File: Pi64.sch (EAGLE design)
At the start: 116 parts, among them J1 USB-MINIB-5PIN, J2 AVR_SPI, J3 FTDI_DEVICERA_SMT, J4 FTDI_DEVICERA_SMT, SW1 LEFT, SW2 RIGHT, SW3 PWR_SWITCH, SW8 OS102011MA1Q, U1 MIC7221, U2 MCP1642B-ADJ, U3 PAM2306AYPKE, U4 LM4875, U5 Mic5365-2.8Y, U7 AZV321, X2 HEADPHONE

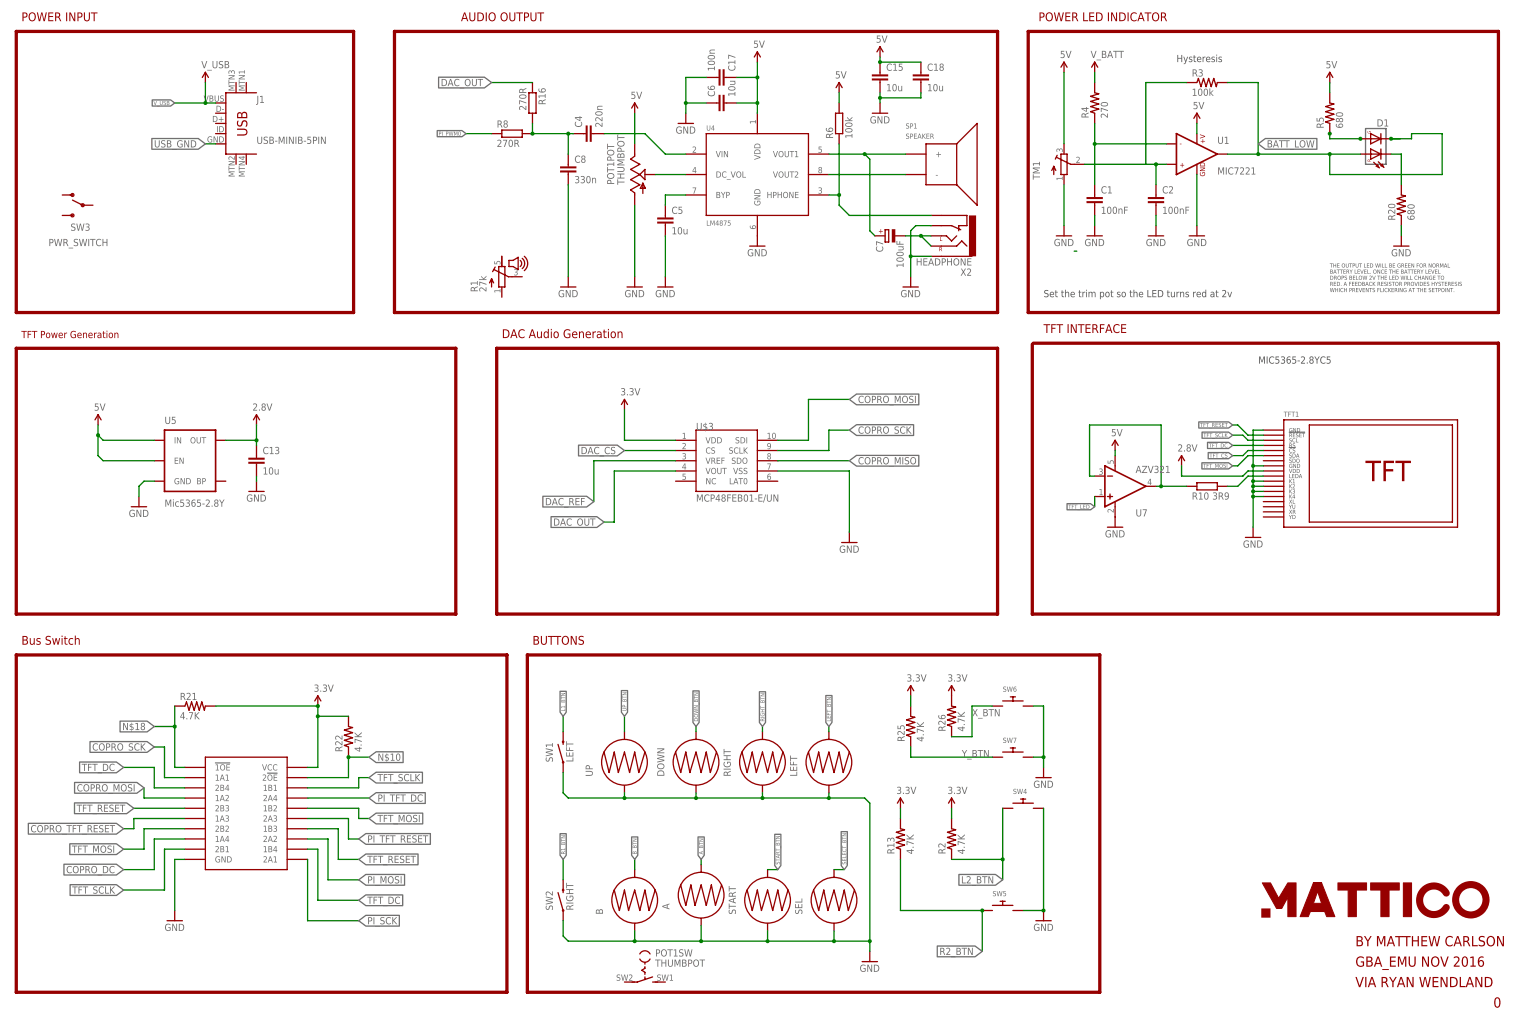
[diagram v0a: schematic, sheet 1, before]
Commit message: removed a lot of cruft and added STM32F
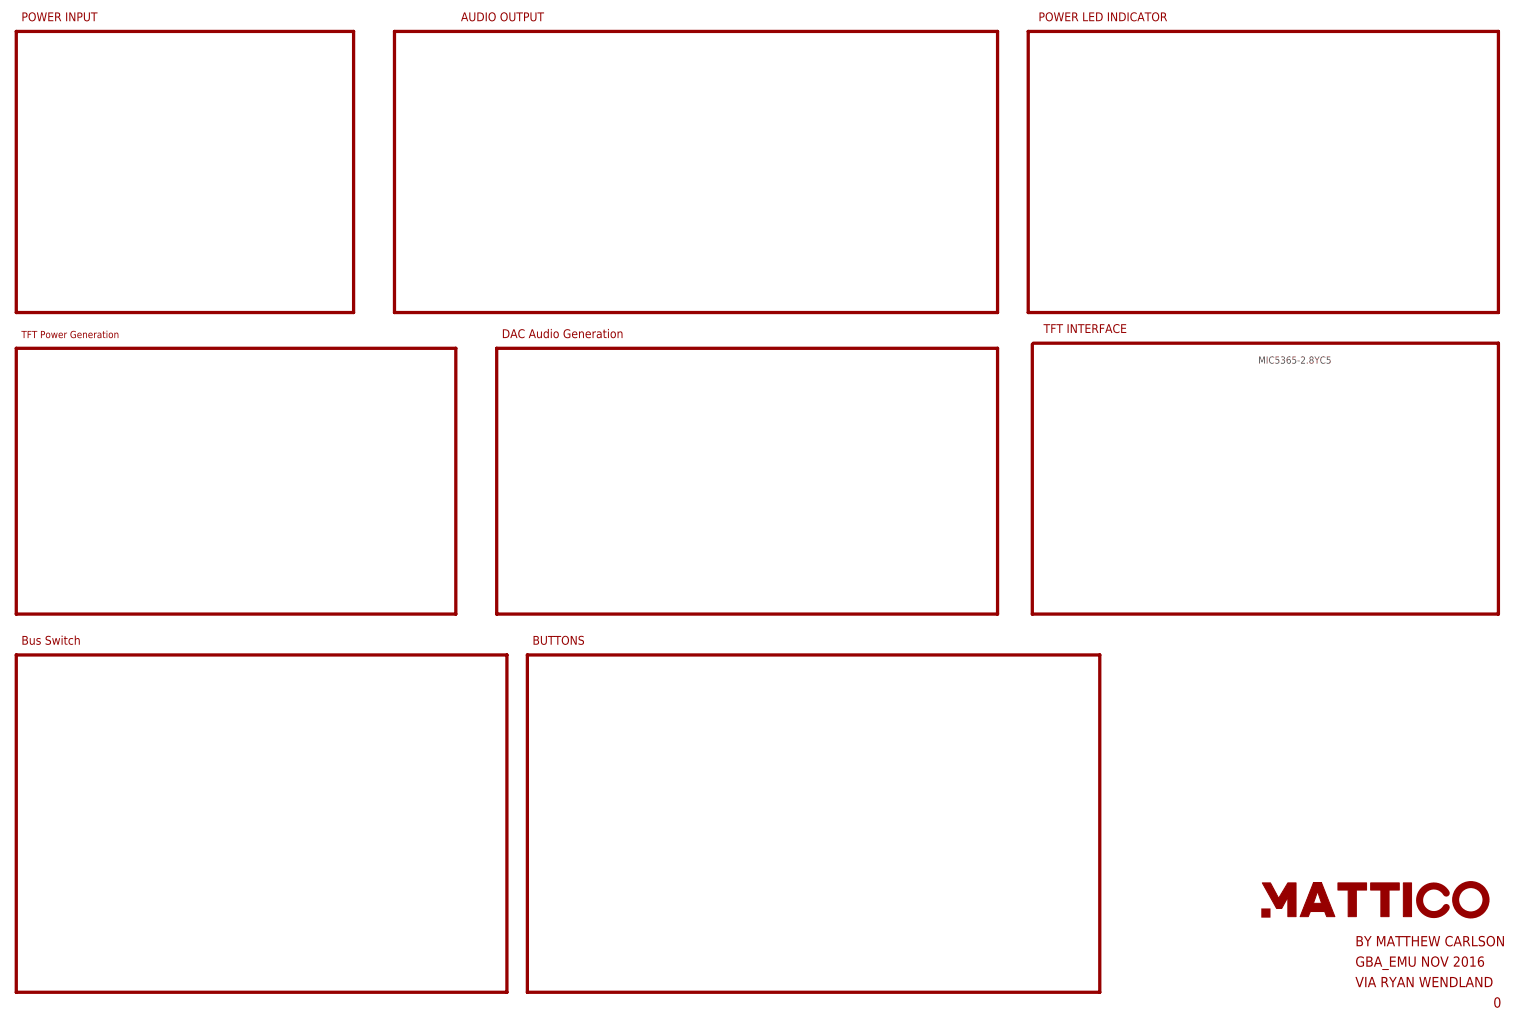
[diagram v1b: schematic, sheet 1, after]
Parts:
- removed A, B, DOWN, LEFT, RIGHT, UP: GBA_BTN_CONDUCTIVE, GBA:GBA_BTN_CONDUCTIVE
- removed BT1: (no value), custom:GBA_BATTERY
- removed C1, C2: 100nF, SparkFun-Capacitors:CAP0603-CAP
- removed C10: 1.0uF, SparkFun-Capacitors:1.0UF-16V-10%(0603)
- removed C11, C12: 22pF, SparkFun-Capacitors:22PF-50V-5%(0603)
- removed C13, C15, C18, C5, C6: 10u, rcl:C-EUC0805
- removed C14, C16: 47uF, SparkFun-Capacitors:47UF-10V-10%(TANT)
- removed C17: 100n, rcl:C-EUC0805
- removed C19: 100nF, SparkFun-Capacitors:10NF/10000PF-50V-10%(0603)
- removed C20, C21, C22, C23: 10uF, SparkFun-Capacitors:10UF-6.3V-20%(0603)
- removed C3: 100nF, SparkFun-Capacitors:10PF-50V-5%(0603)
- removed C4: 220n, rcl:C-EUC0805
- removed C7: 100uF, rcl:CPOL-EU153CLV-0405
- removed C8: 330n, rcl:C-EUC0805
- removed COPRO: MEGA16u2, adafruit:ATMEGA32U2-TQFP
- removed D1: DUAL_LED, custom:DUAL_LED
- removed D2, D3, D4, D7, D8: (no value), adafruit:DIODESOD-523
- removed D5, D6: DIODE_DFLS130L, custom:DIODE_DFLS130L
- removed FAN: (no value), SparkFun-Connectors:M02PTH
- removed J1: USB-MINIB-5PIN, SparkFun-Connectors:USB-MINIB-5PIN
- removed J2: AVR_SPI, SparkFun-Connectors:AVR_SPI_PRG_6PTH
- removed J3, J4: FTDI_DEVICERA_SMT, SparkFun-Connectors:FTDI_DEVICERA_SMT
- removed L1: 4.7uH, SparkFun-Passives:INDUCTORINDUCTOR_4.7UH
- removed L2, L3: 4.7µH/±30%/1.2A, SparkFun-Coils:INDUCTOR-CDRH-4.7UH
- removed POT1: THUMBPOT, adafruit:THUMBPOT
- removed R$1: 976kR, SparkFun-Resistors:820KOHM-1/10W-1%(0603)
- removed R$8: 430kR, SparkFun-Resistors:820KOHM-1/10W-1%(0603)
- removed R1: 27k, GBA:VOLUME
- removed R10: 3R9, rcl:R-EU_R0805
- removed R12: 1K, SparkFun-Resistors:1KOHM-1/10W-1%(0603)
- removed R13, R2, R21, R22, R25, R26: 4.7K, SparkFun-Resistors:4.7KOHM-1/10W-1%(0603)
- removed R16, R8: 270R, rcl:R-EU_R0805
- removed R17, R18: 22, SparkFun-Resistors:22OHM1/10W1%(0603)
- removed R19, R24, R27, R28: 10K, SparkFun-Resistors:10KOHM-1/10W-1%(0603)0603
- removed R20, R5: 680, SparkFun-Resistors:680OHM1/10W5%(0603)
- removed R23, R29, R3: 100k, SparkFun-Resistors:100KOHM-1/10W-1%(0603)
- removed R30, R31: (no value), SparkFun-Resistors:RESISTOR0805-RES
- removed R4: 270, SparkFun-Resistors:287OHM-1/10W-1%(0603)
- removed R6: 100k, rcl:R-EU_R0805
- removed SEL, START: BUTTON-CONDUCTIVESMD, SparkFun-Electromechanical:BUTTON-CONDUCTIVESMD
- removed SP1: SPEAKER, GBA:SPEAKER
- removed SW1: LEFT, GBA:BUTTON
- removed SW2: RIGHT, GBA:BUTTON
- removed SW3: PWR_SWITCH, GBA:PWR_SWITCH
- removed SW4, SW5: (no value), adafruit:SWITCH_PUSHBUTTONEVQ-PE
- removed SW6, SW7: (no value), adafruit:SWITCH_PUSHBUTTONSOFTTOUCHSMD_SJ
- removed SW8: OS102011MA1Q, adafruit:OS102011MA1Q
- removed T1: (no value), custom:TRANSISTOR_PNP_DRIVERMUN2111T1SC59-BEC
- removed TFT1: GBA_TFT, GBA:GBA_TFT
- removed TM1: (no value), adafruit:TRIMPOTTC33X
- removed U$1: CBT3244AD, custom:CBT3244AD
- removed U$3: MCP48FEB01-E/UN, custom:MCP48FEB01-E/UN
- removed U$5: CRYSTAL-ABLS, custom:CRYSTAL-ABLS
- removed U2: MCP1642B-ADJ, custom:MICROCHIP_MCP1642B-ADJ
- removed U3: PAM2306AYPKE, custom:PAM2306AYPKE
- removed U4: LM4875, texas:LM4875
- removed U5: Mic5365-2.8Y, SparkFun-PowerIC:V_REG_LDOSMD2
- removed U7: AZV321, GBA:AZV321
- removed X1: (no value), Adafruit_PowerBoost:MICROBUILDER_USB_TYPEAPTHFML
- removed X2: HEADPHONE, GBA:HEADPHONE
- U1: value MIC7221 -> STM32F103CBT6; device custom:SPARKFUN-ANALOGIC_MIC7221 -> custom:STM32F103CBT6
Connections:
- removed net BATT_LOW: D1.1, D1.3, D8.A, R3.2, U1.OUT1
- removed net COPRO_D+: R18.1
- removed net COPRO_D-: R17.1
- removed net COPRO_DC: COPRO.PB6(PCINT6), U$1.1A4
- removed net COPRO_MISO: COPRO.PB3(PDO/MISO/PCINT3), J2.1, U$3.SDO
- removed net COPRO_MOSI: COPRO.PB2(PDI/MOSI/PCINT2), J2.4, U$1.1A2, U$3.SDI
- removed net COPRO_RESET: COPRO./RESET(PC1), J2.5, R19.1
- removed net COPRO_RX: COPRO.PD2(INT2/AIN1/RXD1)
- removed net COPRO_SCK: COPRO.PB1(SCK/PCINT1), J2.3, U$1.1A1, U$3.SCLK
- removed net COPRO_TFT_RESET: COPRO.PB0(SS/PCINT0), U$1.1A3
- removed net COPRO_TX: COPRO.PD3(INT3/TXD1)
- removed net DAC_CS: COPRO.PB5(PCINT5), U$3.CS
- removed net DAC_OUT: R16.1, U$3.VOUT
- removed net DAC_REF: U$3.VREF
- removed net FAN_EN: R12.2
- removed net N$10: R22.1, U$1.2!OE
- removed net N$11: C5.1, U4.BYP
- removed net N$12: COPRO.PC2(AIN2/PCIN11), R28.1
- removed net N$13: C7.-, X2.LEFT, X2.RIGHT
- removed net N$14: C7.+, SP1.+, U4.VOUT1
- removed net N$15: SP1.-, U4.VOUT2
- removed net N$16: R6.1, U4.HPHONE, X2.2
- removed net N$18: R21.1, U$1.!1OE
- removed net N$19: COPRO.D-, R17.2
- removed net N$2: C4.1, C8.1, R16.2, R8.2
- removed net N$21: R10.2, TFT1.LEDA
- removed net N$22: COPRO.D+, R18.2
- removed net N$23: R$1.1, R$8.2, U2.VFB
- removed net N$24: R10.1, U7.-IN, U7.OUT
- removed net N$25: C10.1, COPRO.UCAP
- removed net N$28: C11.1, COPRO.XTAL1, U$5.P$2
- removed net N$29: C12.1, COPRO.XTAL2/PC0, U$5.P$1
- removed net N$3: D7.A, D8.C
- removed net N$31: D3.A, D4.C
- removed net N$32: L3.1, U3.LX2
- removed net N$33: D3.C, D7.C, R27.2, R28.2
- removed net N$34: L1.2, U2.SW
- removed net N$38: COPRO.PC7(ICP1/INT4/CLKO), R27.1
- removed net N$39: FAN.1, T1.C
- removed net N$4: C2.1, R3.1, TM1.S, U1.+IN1
- removed net N$40: R12.1, T1.B
- removed net N$44: COPRO.PD0(INT0/OC0B), R24.1
- removed net N$45: C14.+, D5.C, D6.C, L1.1, SW8G$1.P, U2.VIN
- removed net N$46: C19.1, R29.1, U3.EN2
- removed net N$47: L2.1, U3.LX1
- removed net N$49: R31.2, U3.FB1
- removed net N$5: C1.1, R4.1, U1.-IN1
- removed net N$50: R30.1, U3.FB2
- removed net N$6: D1.4, R5.1
- removed net N$7: D1.2, R20.2
- removed net N$8: POT1POT.S, U4.DC_VOL
- removed net N$9: C4.2, U4.VIN
- removed net PWR_DOWN: D2.A, D4.A, SW8G$1.S
- removed net PWR_UP: D2.C, R23.2, R24.2, U2.EN
- removed net TFT_CS: COPRO.PD4(INT5/AIN3), TFT1.!CS
- removed net TFT_DC: TFT1.RS, U$1.1B4, U$1.2B4
- removed net TFT_MOSI: TFT1.SDA, U$1.1B2, U$1.2B2
- removed net TFT_RESET: TFT1.!RESET, U$1.1B3, U$1.2B3
- removed net TFT_SCLK: TFT1.SCL, U$1.1B1, U$1.2B1
- removed net USB_GND: J1.GND
- removed net V_BATT: BT1.+, D6.A, R4.2
- removed net V_USB: D5.A, J1.VBUS
- new net +3V3: U1.VBAT, U1.VDDA, U1.VDD_1, U1.VDD_2, U1.VDD_3
- net 1.8V: no longer C20.1, L3.2, R30.2
- net 2.8V: no longer C13.1, TFT1.VDD, U5.OUT
- net 3.3V: no longer C21.1, COPRO.AVCC, COPRO.UVCC, COPRO.VCC, L2.2, R13.2, R2.2, R21.2, R22.2, R25.2, R26.2, R31.1, U$1.VCC, U$3.VDD
- net 5V: no longer C15.1, C16.+, C17.1, C18.1, C22.1, C23.1, C3.1, C6.2, FAN.2, J2.2, POT1POT.E, R$1.2, R19.2, R29.2, R5.2, R6.2, TM1.E, U1.+V, U2.VOUT, U3.EN1, U3.VIN1, U3.VIN2, U4.VDD, U5.EN, U5.IN, U7.V+, X1.VBUS
- net A_BTN: no longer A.2
- net B_BTN: no longer B.2
- net DOWN_BTN: no longer DOWN.2
- net GND: no longer A.1, B.1, BT1.-, C1.2, C10.2, C11.2, C12.2, C13.2, C14.-, C15.2, C16.-, C17.2, C18.2, C19.2, C2.2, C20.2, C21.2, C22.2, C23.2, C3.2, C5.2, C6.1, C8.2, COPRO.GND, COPRO.UGND, DOWN.1, J2.6, J3.GND, J4.GND, LEFT.1, POT1POT.A, R$8.1, R20.1, R23.1, RIGHT.1, SEL.1, START.1, SW1.1, SW2.1, SW4.P$2, SW5.P$2, SW6.P$2, SW7.P$2, T1.E, TFT1.GND@1, TFT1.GND@2, TFT1.K1, TFT1.K2, TFT1.K3, TFT1.K4, TM1.A, U$1.GND, U$3.VSS, U1.GND, U2.GND, U3.GND@1, U3.GND@2, U4.GND, U5.GND, U7.V-, UP.1, X1.GND, X2.1, X2.GND
- net L1_BTN: no longer SW1.2
- net L2_BTN: no longer R2.1, SW4.P$1
- net LEFT_BTN: no longer LEFT.2
- net PI_MOSI: no longer U$1.2A2
- net PI_PWM0: no longer R8.1
- net PI_SCK: no longer U$1.2A1
- net PI_TFT_DC: no longer U$1.2A4
- net PI_TFT_RESET: no longer U$1.2A3
- net R1_BTN: no longer SW2.2
- net R2_BTN: no longer R13.1, SW5.P$1
- net RIGHT_BTN: no longer RIGHT.2
- net SELECT_BTN: no longer SEL.2
- net START_BTN: no longer START.2
- net TFT_LED: no longer U7.+IN
- net UP_BTN: no longer UP.2
- net X_BTN: no longer R26.1, SW6.P$1
- net Y_BTN: no longer R25.1, SW7.P$1
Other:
- note removed: "C16 as close to VOUT as possible"
- note removed: "Hysteresis"
- note removed: "Power Or'ing"
- note removed: "Set the trim pot so the LED turns red at 2v"
- note removed: "THE OUTPUT LED WILL BE GREEN FOR NORMAL BATTERY LEVEL. ONCE THE BATTERY LEVEL DROPS BELOW 2V THE LED WILL CHANGE TO RED. A FEEDBACK RESISTOR PROVIDES HYSTERESIS WHICH PREVENTS FLICKERING AT THE SETPOINT."
- moved on the sheet: TP1, TP2, TP3, TP4, TP5, TP6, TP7

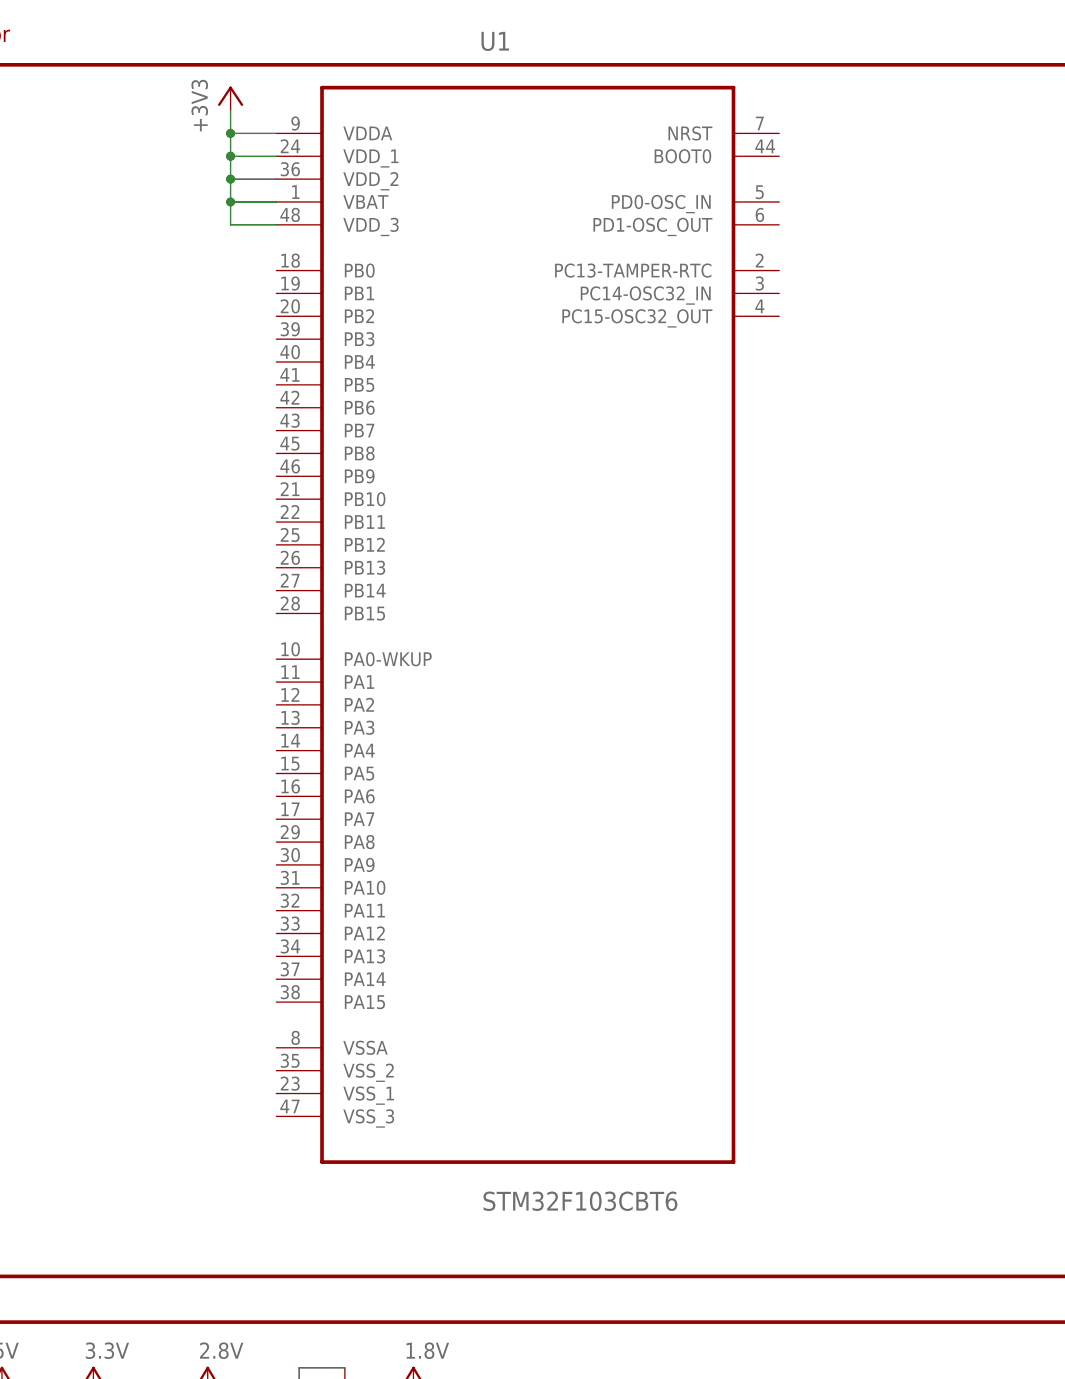
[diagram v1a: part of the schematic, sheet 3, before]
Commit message: Added PWR and GND to STM32
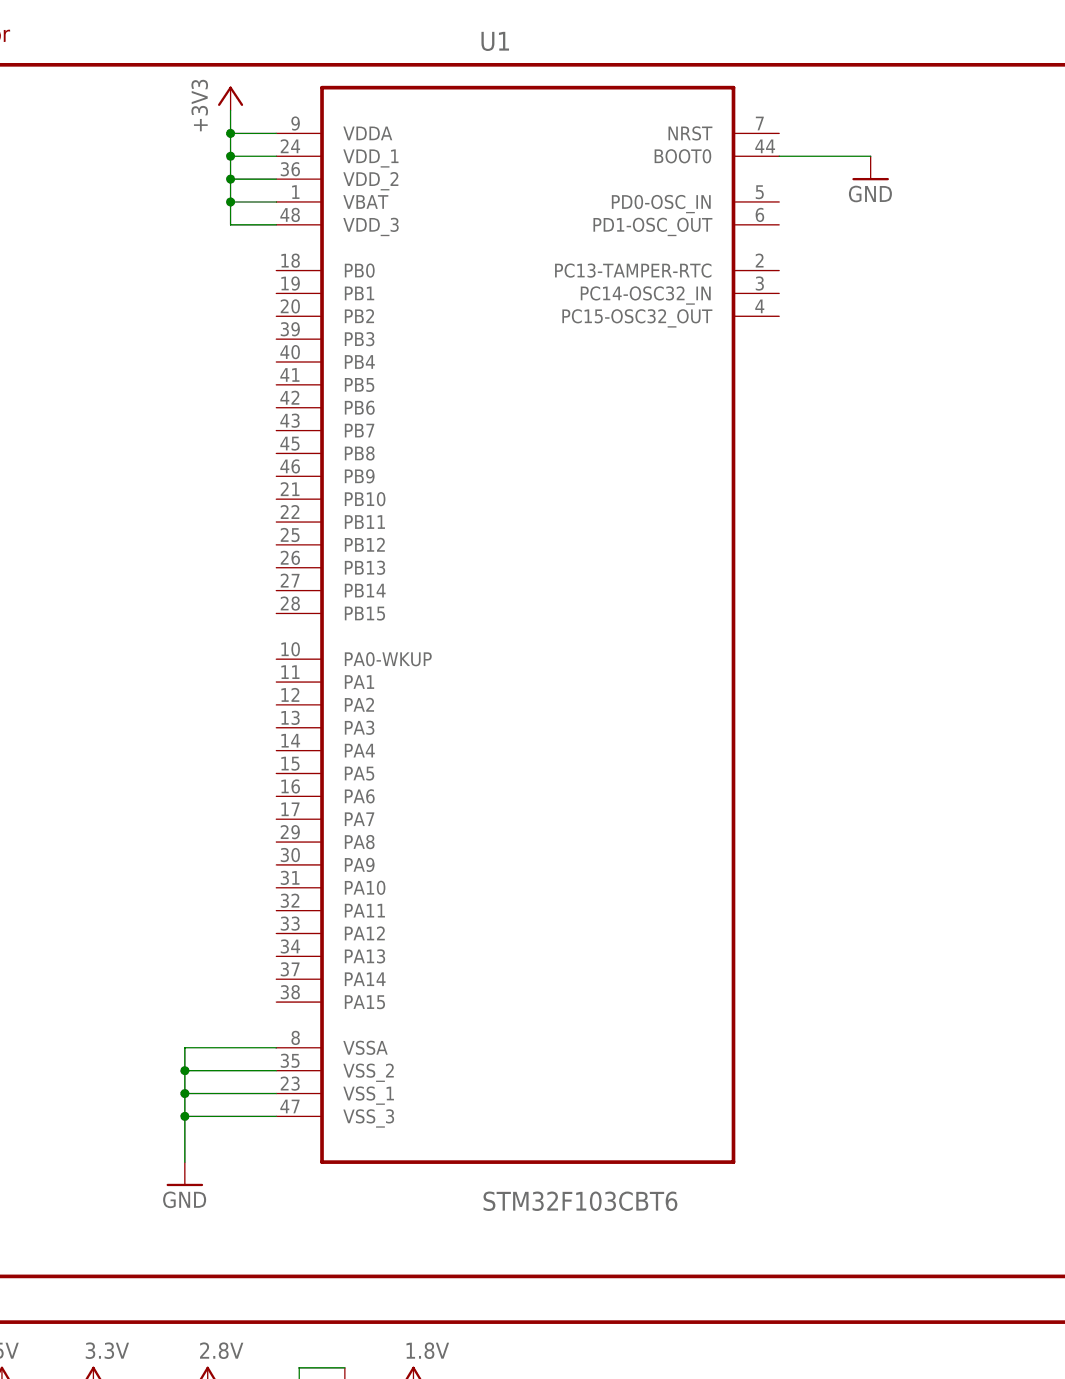
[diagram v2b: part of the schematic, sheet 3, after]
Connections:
- net GND: now also U1.BOOT0, U1.VSSA, U1.VSS_1, U1.VSS_2, U1.VSS_3
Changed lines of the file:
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@@
 <part name="U1" library="custom" deviceset="STM32F103CBT6" device=""/>
 <part name="3V3_STM" library="supply1" library_urn="urn:adsk.eagle:library:371" deviceset="+3V3" device=""/>
+<part name="GND1" library="SparkFun-Aesthetics" deviceset="GND" device=""/>
+<part name="GND2" library="SparkFun-Aesthetics" deviceset="GND" device=""/>
 </parts>
 <sheets>
@@
 <attribute name="VALUE" x="45.72" y="160.02" size="1.778" layer="96" rot="R90"/>
 </instance>
+<instance part="GND1" gate="1" x="119.38" y="154.94" smashed="yes">
+<attribute name="VALUE" x="116.84" y="152.4" size="1.778" layer="96"/>
+</instance>
+<instance part="GND2" gate="1" x="43.18" y="43.18" smashed="yes">
+<attribute name="VALUE" x="40.64" y="40.64" size="1.778" layer="96"/>
+</instance>
 </instances>
 <busses>
@@
 <wire x1="55.88" y1="22.86" x2="60.96" y2="22.86" width="0.1524" layer="91"/>
 </segment>
-</net>
+<segment>
+<pinref part="U1" gate="A" pin="BOOT0"/>
+<pinref part="GND1" gate="1" pin="GND"/>
+<wire x1="109.22" y1="157.48" x2="119.38" y2="157.48" width="0.1524" layer="91"/>
+</segment>
+<segment>
+<pinref part="U1" gate="A" pin="VSSA"/>
+<wire x1="53.34" y1="58.42" x2="43.18" y2="58.42" width="0.1524" layer="91"/>
+<wire x1="43.18" y1="58.42" x2="43.18" y2="55.88" width="0.1524" layer="91"/>
+<wire x1="43.18" y1="55.88" x2="43.18" y2="53.34" width="0.1524" layer="91"/>
+<wire x1="43.18" y1="53.34" x2="43.18" y2="50.8" width="0.1524" layer="91"/>
+<pinref part="U1" gate="A" pin="VSS_2"/>
+<wire x1="53.34" y1="55.88" x2="43.18" y2="55.88" width="0.1524" layer="91"/>
+<junction x="43.18" y="55.88"/>
+<pinref part="U1" gate="A" pin="VSS_1"/>
+<wire x1="53.34" y1="53.34" x2="43.18" y2="53.34" width="0.1524" layer="91"/>
+<junction x="43.18" y="53.34"/>
+<pinref part="U1" gate="A" pin="VSS_3"/>
+<wire x1="53.34" y1="50.8" x2="43.18" y2="50.8" width="0.1524" layer="91"/>
+<junction x="43.18" y="50.8"/>
+<pinref part="GND2" gate="1" pin="GND"/>
+<wire x1="43.18" y1="50.8" x2="43.18" y2="45.72" width="0.1524" layer="91"/>
+</segment>
+</net>
